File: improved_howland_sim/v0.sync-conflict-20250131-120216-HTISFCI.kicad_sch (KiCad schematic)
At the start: 16 parts, among them U2 ${SIM.PARAMS}, U3 ${SIM.PARAMS}, U4 ${SIM.PARAMS}

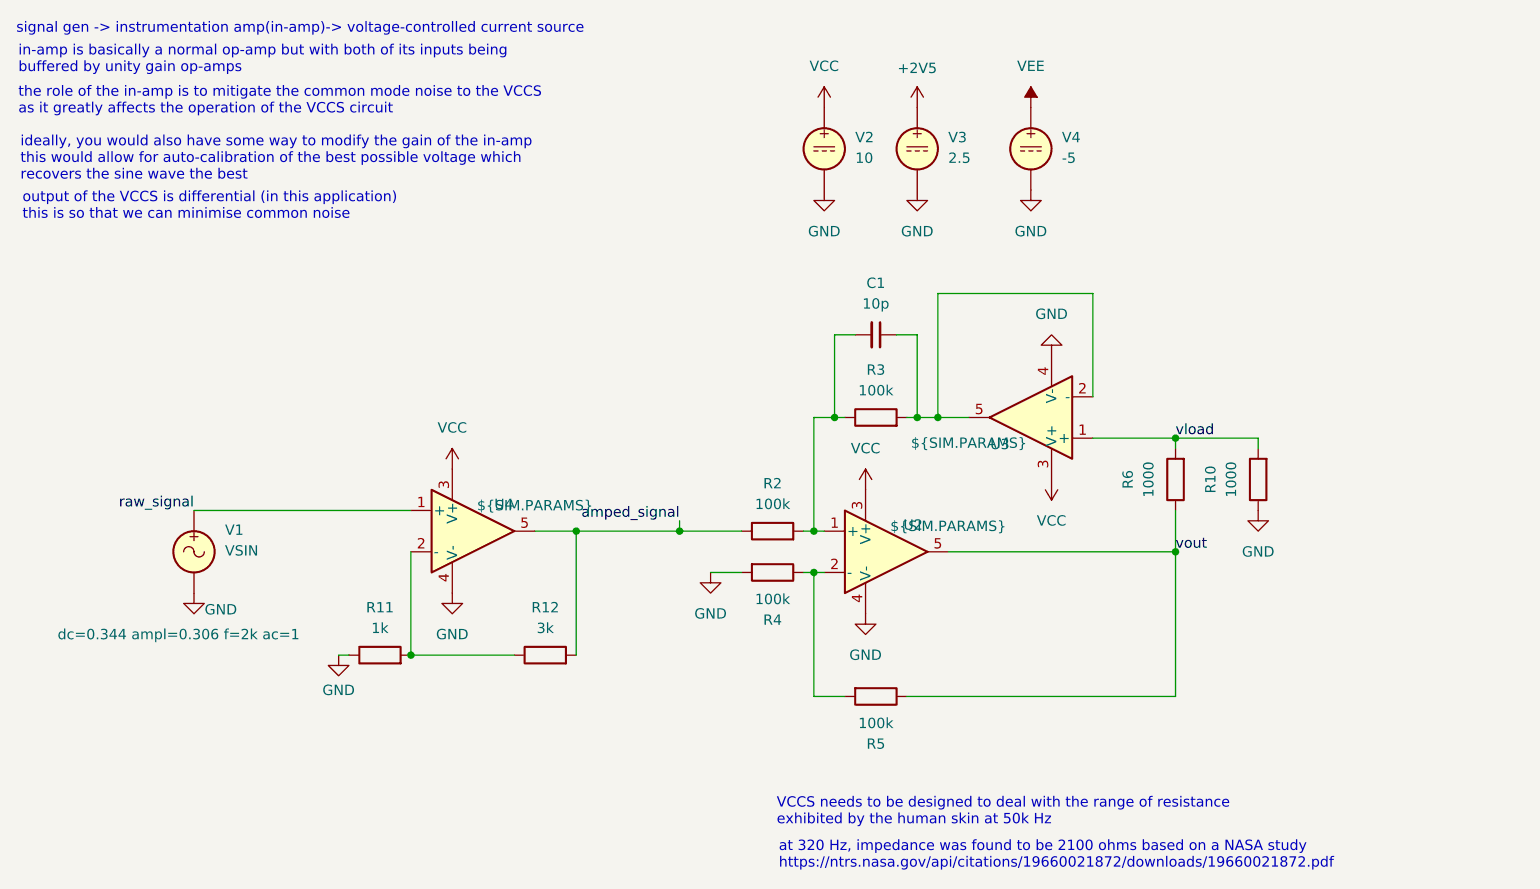
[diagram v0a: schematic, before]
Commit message: esp32-based integration test of the board
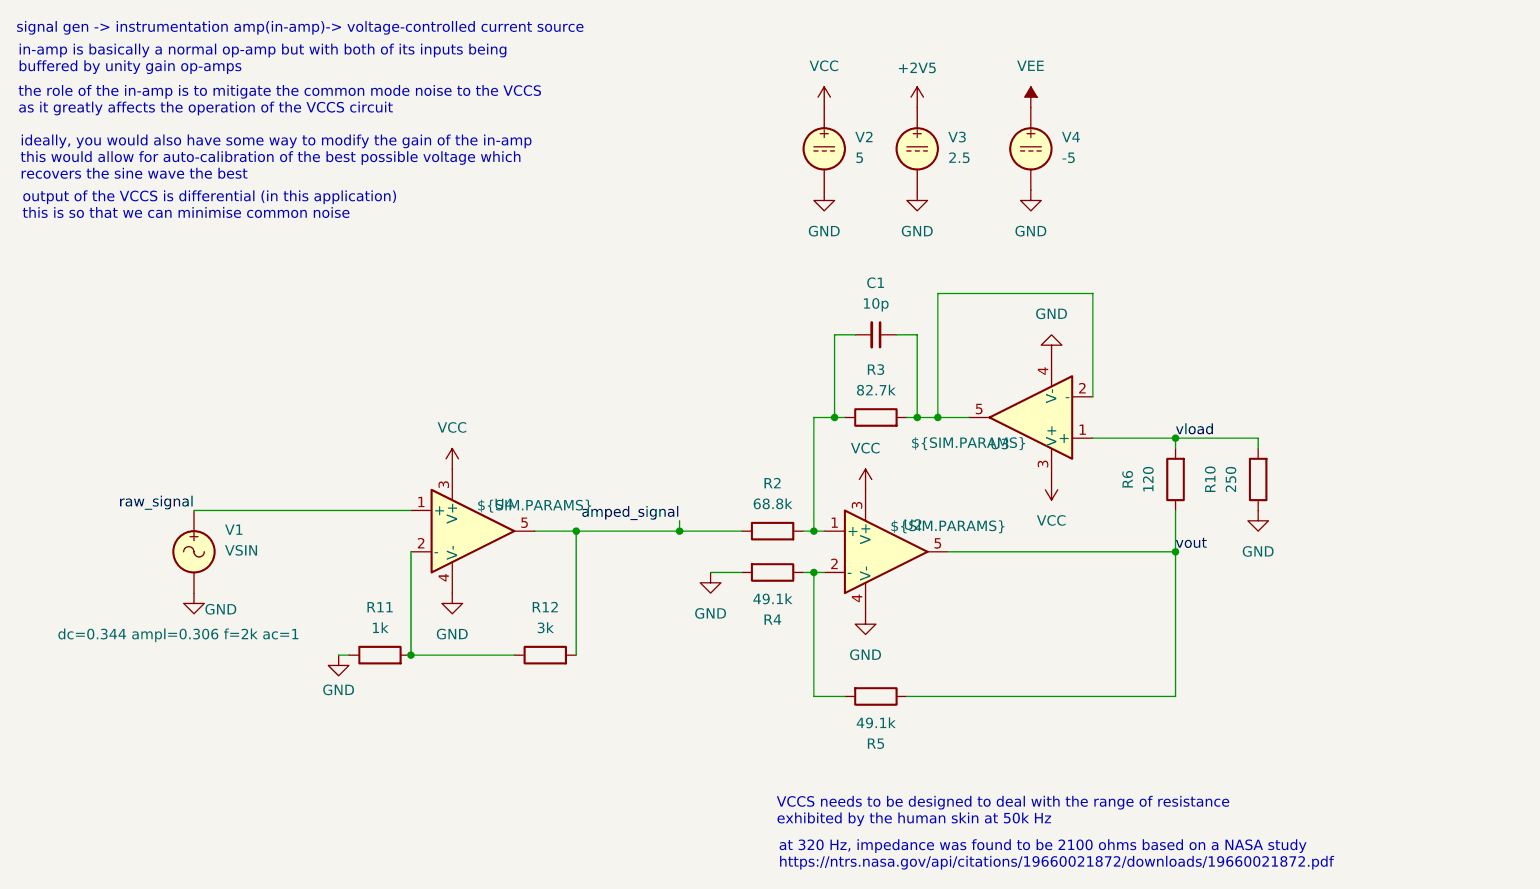
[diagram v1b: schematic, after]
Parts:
- R10: value 1000 -> 250
- R2: value 100k -> 68.8k
- R3: value 100k -> 82.7k
- R4, R5: value 100k -> 49.1k
- R6: value 1000 -> 120
- V2: value 10 -> 5
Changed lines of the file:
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@@
 			)
 		)
-		(property "Value" "100k"
+		(property "Value" "82.7k"
 			(at 120.65 62.738 90)
 			(effects
@@
 			)
 		)
-		(property "Value" "1000"
+		(property "Value" "250"
 			(at 164.338 73.66 90)
 			(effects
@@
 			)
 		)
-		(property "Value" "100k"
+		(property "Value" "49.1k"
 			(at 120.65 103.632 90)
 			(effects
@@
 			)
 		)
-		(property "Value" "10"
+		(property "Value" "5"
 			(at 118.11 34.1601 0)
 			(effects
@@
 			)
 		)
-		(property "Value" "100k"
+		(property "Value" "68.8k"
 			(at 107.95 76.708 90)
 			(effects
@@
 			)
 		)
-		(property "Value" "1000"
+		(property "Value" "120"
 			(at 154.178 73.66 90)
 			(effects
@@
 			)
 		)
-		(property "Value" "100k"
+		(property "Value" "49.1k"
 			(at 107.95 88.392 90)
 			(effects
